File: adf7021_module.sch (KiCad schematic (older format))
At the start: 39 parts

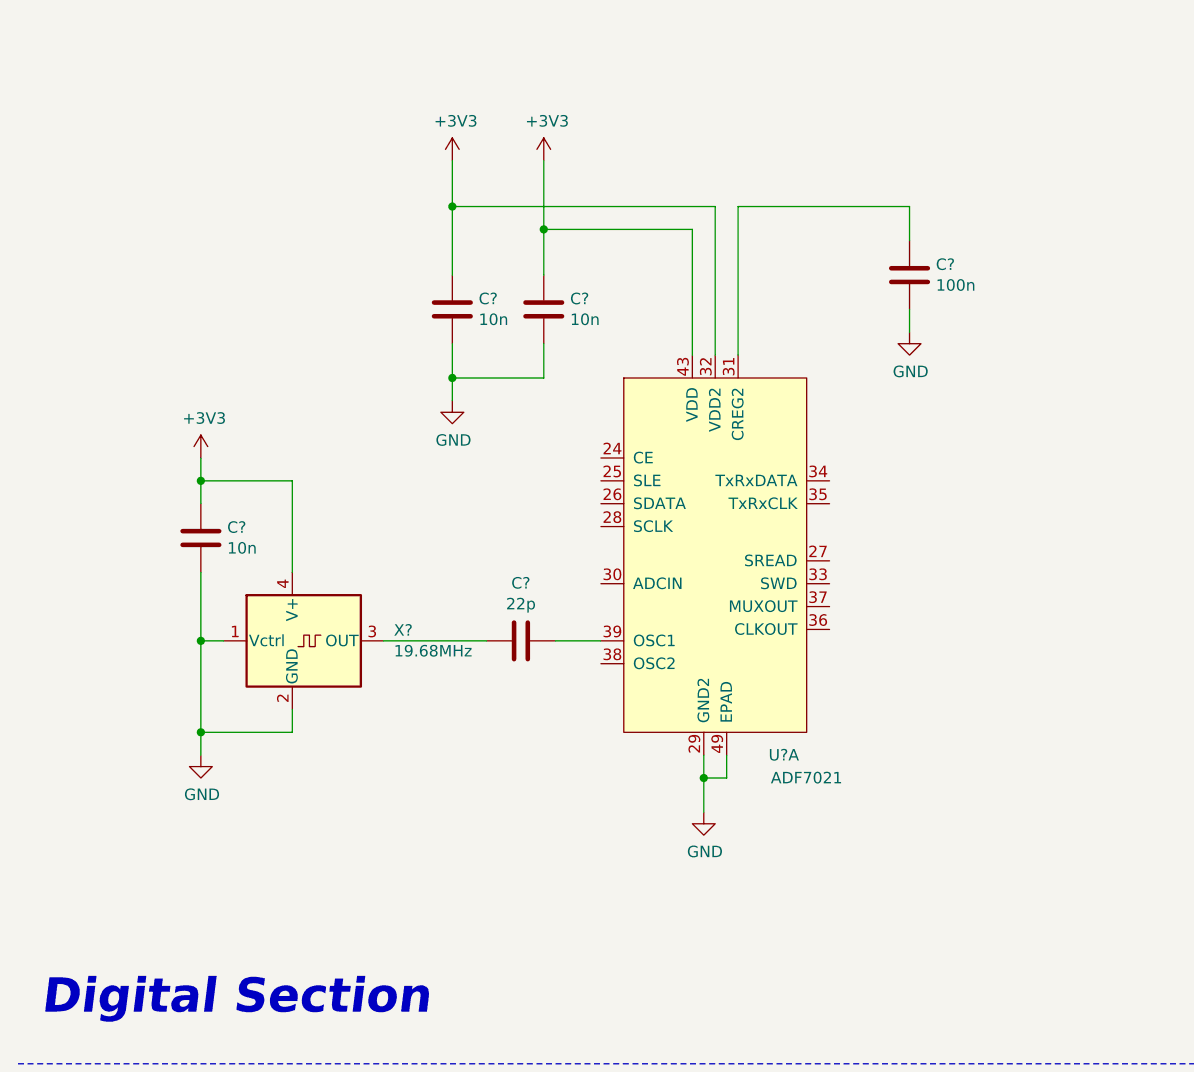
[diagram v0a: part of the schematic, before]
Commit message: Add external clock input SMA
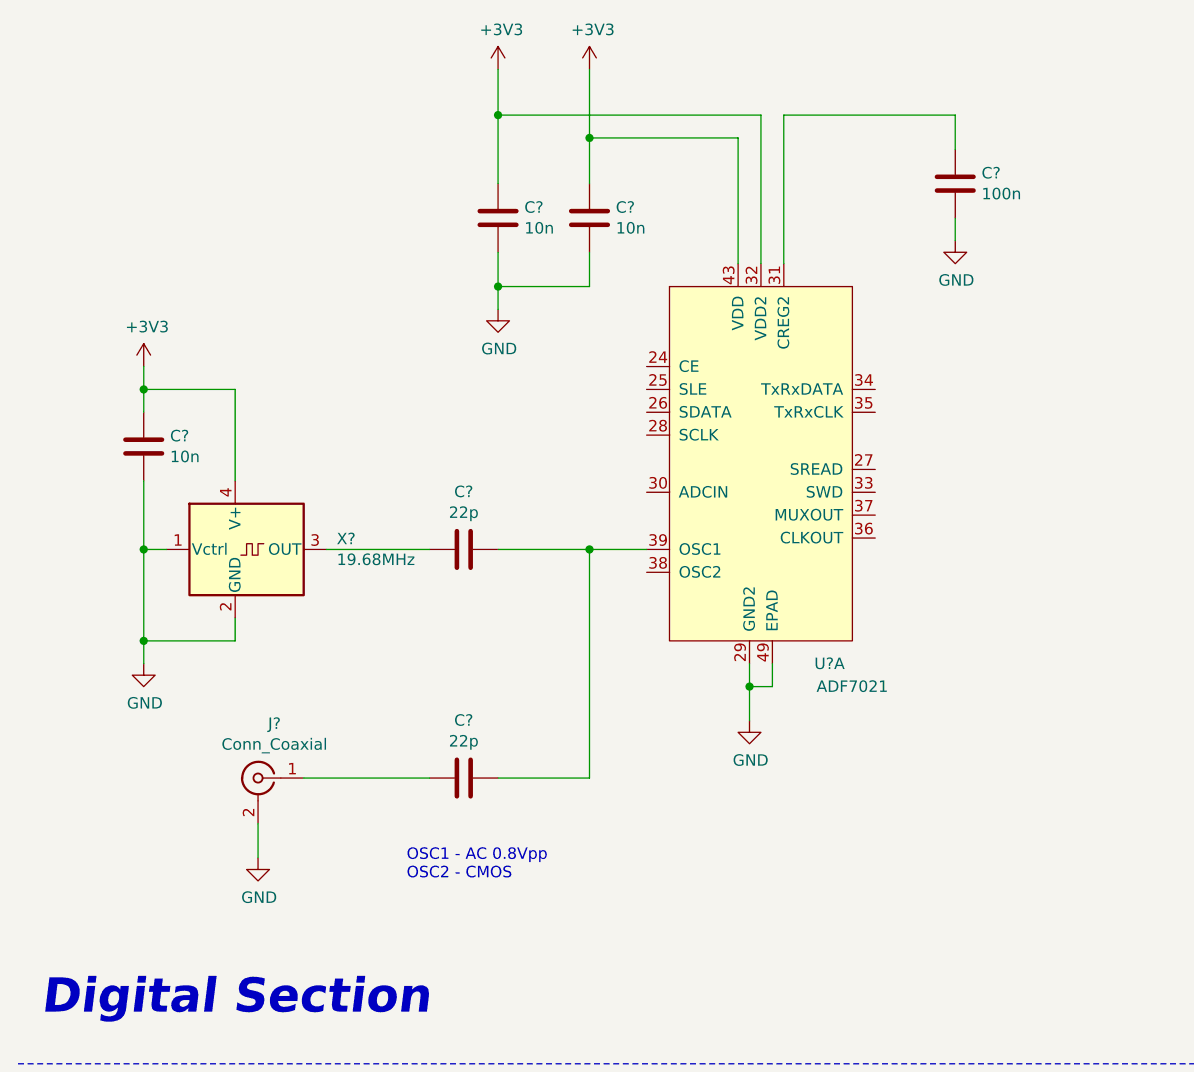
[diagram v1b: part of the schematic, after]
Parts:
- added C?: 22p, symbol Device:C
- added J?: Conn_Coaxial, symbol Connector:Conn_Coaxial
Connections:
- net GND: now also J?.2 (Ext)
- net at C?.1, U?.39 (OSC1): now also C?.1
- new net: C?.2, J?.1 (In)
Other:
- note added: "OSC1 - AC 0.8Vpp\nOSC2 - CMOS"
- moved on the sheet: C?, U?A, X?

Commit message: RF output chain, labels for digital pins
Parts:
- removed J?: Conn_Coaxial, symbol Connector:Conn_Coaxial
- added C16: 100n, symbol Device:C
- added C17: 2.2n, symbol Device:C
- added C18: 10p, symbol Device:C
- added C23, C25: DNP, symbol Device:C
- added C24: 6.8p, symbol Device:C
- added C26, C27: 4.7p, symbol Device:C
- added J2: Conn_Coaxial, symbol Connector:Conn_Coaxial
- added L2: 20n, symbol Device:L
- added L3: 22n, symbol Device:L
- added R4: 100, symbol Device:R
- added R5, R6: 47k, symbol Device:R
- added R7: 22k, symbol Device:R
- gave numbers to parts that had none: 38
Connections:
- net RFIN is gone; now on an unnamed net: C30.2
- net GND: now also C17.1, C23.2, C24.2, C25.2, J2.2 (Ext), R7.1
- net VCOIN: now also R4.1, R5.2; no longer C12.1, R2.2
- net at C15.2: now also C9.1, U1.39 (OSC1)
- net CE: now reaches U1.24 (CE)
- net SLE: now reaches U1.25 (SLE)
- net SDATA: now reaches U1.26 (SDATA)
- net SREAD: now reaches U1.27 (SREAD)
- net SCLK: now reaches U1.28 (SCLK)
- net ADCIN: now reaches U1.30 (ADCIN)
- net SWD: now reaches U1.33 (SWD)
- net TxRxData: now reaches U1.34 (TxRxDATA)
- net TxRxCLK: now reaches U1.35 (TxRxCLK)
- net CLKOUT: now reaches U1.36 (CLKOUT)
- net MUXOUT: now reaches U1.37 (MUXOUT)
- net at C19.2, L4.2, U1.4 (RFOUT): now also C18.2
- net at L5.2, U1.6 (RFIN): now also C26.1, C27.1; no longer C30.1
- net at C33.1, J3.1 (In), L7.1: now also C27.2
- net at C31.1, L6.2: now also C30.1
- net RFOUT: no longer names the net of C19.1
- net RFOUT: now also C23.1, C26.2, L2.2
- new net: C18.1, C25.1, J2.1 (In), L3.1
- new net: C24.1, L2.1, L3.2
- new net: C12.1, R2.2, R4.2
- new net: C16.2, R5.1
- new net: C16.1, C17.2, R6.2
- new net CLK_AC_IN: C15.1
- new net FM_MOD: R6.1, R7.2
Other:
- note added: "C18, C19 are "multiplexer"\nDC blocking caps. Place one."
- note added: "C26, C27, C30 are "multiplexer"\nDC blocking caps. Place one."
- note added: "Input 3Vp-p\nSet deviation with R5"
- note added: "OSC1 - AC 0.8Vp-p\nOSC2 - CMOS"
- note removed: "OSC1 - AC 0.8Vpp\nOSC2 - CMOS"
- moved on the sheet: C10, C11, C12, C13, C14, C15, C19, C2, C20, C21, C22, C28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

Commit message: Improving documentation on schematic
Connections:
- net RFIN: now reaches C26.1, C27.1, C30.2, L5.2, U1.6 (RFIN)
- net RFOUT: now reaches C18.2, C19.2, L4.2, U1.4 (RFOUT)
- net CLK_DC_IN: now reaches U1.38 (OSC2)
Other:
- note added: "C18, C19 are "multiplexer"\nDC blocking caps. Place one.\n\nC18 - Bypass\nC19 - Filter output"
- note added: "C26, C27, C30 are "multiplexer"\nDC blocking caps. Place one.\n\nC26 - Shared Tx/Rx\nC27 - Bypass Rx\nC30 - Filter Rx"
- note added: "C9, C15 are "multiplexer"\nDC blocking caps. Place one.\n\nC9 - TXCO Input\nC15 - External Input"
- note added: "Harmonic filter values taken from EVAL-ADF7021DBZ3\nmodule. (For 431 MHz - 470 MHz)\n\n3 dB @ 730 MHz"
- note removed: "3 dB @ 730 MHz"
- note removed: "C18, C19 are "multiplexer"\nDC blocking caps. Place one."
- note removed: "C26, C27, C30 are "multiplexer"\nDC blocking caps. Place one."
- note removed: "Harmonic filter values taken from EVAL-ADF7021DBZ3\nmodule. (For 431 MHz - 470 MHz)"
- moved on the sheet: C15, C9
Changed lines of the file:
@@
 AR Path="/5FB73817/6009402F" Ref="X?"  Part="1"
 AR Path="/6009402F" Ref="X1"  Part="1"
-F 0 "X1" H 1694 3296 50  0000 L CNN
-F 1 "19.68MHz" H 1694 3205 50  0000 L CNN
+F 0 "X1" H 1350 3650 50  0000 L CNN
+F 1 "19.68MHz" H 1350 3550 50  0000 L CNN
 F 2 "Oscillator:Oscillator_SMD_Fordahl_DFAS2-4Pin_7.3x5.1mm" H 2350 2900 50  0001 C CNN
 F 3 "http://www.metatech.com.hk/product/fordahl/pdf/2002%20TCXO%20Page%2043-58.pdf" H 1150 3250 50  0001 C CNN
@@
 L Device:C C?
 U 1 1 60094035
-P 2250 3250
+P 2150 3250
 AR Path="/5FB73817/60094035" Ref="C?"  Part="1"
 AR Path="/60094035" Ref="C9"  Part="1"
-F 0 "C9" V 1998 3250 50  0000 C CNN
-F 1 "22p" V 2089 3250 50  0000 C CNN
-F 2 "" H 2288 3100 50  0001 C CNN
-F 3 "~" H 2250 3250 50  0001 C CNN
-	1    2250 3250
+F 0 "C9" V 1898 3250 50  0000 C CNN
+F 1 "22p" V 1989 3250 50  0000 C CNN
+F 2 "" H 2188 3100 50  0001 C CNN
+F 3 "~" H 2150 3250 50  0001 C CNN
+	1    2150 3250
 	0    1    1    0
 $EndComp
-Wire Wire Line
-	1650 3250 2100 3250
 $Comp
 L power:+3V3 #PWR?
@@
 	9400 9150 9400 9550
 Connection ~ 9400 9550
-Text Notes 8750 8650 2    50   ~ 0
-3 dB @ 730 MHz
 Wire Notes Line
 	6700 1000 6700 5500
@@
 Text Notes 9900 4600 0    50   Italic 0
 Loop filter taken from EVAL-ADF7021DBZ3\nmodule. (For 431 MHz - 470 MHz)
-Text Notes 9300 6000 2    50   Italic 0
-Harmonic filter values taken from EVAL-ADF7021DBZ3\nmodule. (For 431 MHz - 470 MHz)
+Text Notes 7000 10050 0    50   Italic 0
+Harmonic filter values taken from EVAL-ADF7021DBZ3\nmodule. (For 431 MHz - 470 MHz)\n\n3 dB @ 730 MHz
 Text Notes 2000 9850 0    50   Italic 0
 Matching network taken from EVAL-ADF7021DBZ3\nmodule. (For 431 MHz - 470 MHz)
@@
 L Device:C C?
 U 1 1 5FC62852
-P 2600 3500
+P 2450 3500
 AR Path="/5FB73817/5FC62852" Ref="C?"  Part="1"
 AR Path="/5FC62852" Ref="C15"  Part="1"
-F 0 "C15" V 2348 3500 50  0000 C CNN
-F 1 "22p" V 2439 3500 50  0000 C CNN
-F 2 "" H 2638 3350 50  0001 C CNN
-F 3 "~" H 2600 3500 50  0001 C CNN
-	1    2600 3500
+F 0 "C15" V 2198 3500 50  0000 C CNN
+F 1 "22p" V 2289 3500 50  0000 C CNN
+F 2 "" H 2488 3350 50  0001 C CNN
+F 3 "~" H 2450 3500 50  0001 C CNN
+	1    2450 3500
 	-1   0    0    1
 $EndComp
-Text Notes 2550 4700 0    50   ~ 0
+Text Notes 2200 4350 0    50   ~ 0
 OSC1 - AC 0.8Vp-p\nOSC2 - CMOS
 $Comp
@@
 	14400 4400 14700 4400
 Connection ~ 14400 4400
-Text Label 14700 4400 0    50   ~ 0
-FM_MOD
 Text Notes 14650 4200 0    50   ~ 0
 Input 3Vp-p\nSet deviation with R5
@@
 	9400 7250 9400 7650
 Connection ~ 9400 7650
-Text Notes 8750 6750 2    50   ~ 0
-3 dB @ 730 MHz
 Wire Wire Line
 	6000 7900 6000 7050
@@
 	1250 7850 1250 10150
 Wire Wire Line
-	1250 10150 6050 10150
-Wire Wire Line
-	6050 10150 6050 8950
-Wire Wire Line
-	6050 8950 6450 8950
+	1250 10150 5800 10150
+Wire Wire Line
+	5800 10150 5800 8950
+Wire Wire Line
+	5800 8950 6450 8950
 Connection ~ 7300 8950
 Wire Wire Line
@@
 Wire Wire Line
 	9000 7050 8700 7050
-Text Notes 6350 10150 0    50   ~ 0
-C26, C27, C30 are "multiplexer"\nDC blocking caps. Place one.
-Text Notes 5850 6000 0    50   ~ 0
-C18, C19 are "multiplexer"\nDC blocking caps. Place one.
-Wire Wire Line
-	2600 3250 3600 3250
-Wire Wire Line
-	2400 3250 2600 3250
-Connection ~ 2600 3250
-Wire Wire Line
-	2600 3350 2600 3250
-Wire Wire Line
-	2600 3650 2600 3750
-Wire Wire Line
-	2600 3750 2000 3750
+Text Notes 6100 9650 0    30   ~ 0
+C26, C27, C30 are "multiplexer"\nDC blocking caps. Place one.\n\nC26 - Shared Tx/Rx\nC27 - Bypass Rx\nC30 - Filter Rx
+Text Notes 5800 6100 0    30   ~ 0
+C18, C19 are "multiplexer"\nDC blocking caps. Place one.\n\nC18 - Bypass\nC19 - Filter output
+Wire Wire Line
+	2450 3250 3600 3250
+Wire Wire Line
+	2300 3250 2450 3250
+Connection ~ 2450 3250
+Wire Wire Line
+	2450 3350 2450 3250
+Wire Wire Line
+	2450 3650 2450 3750
+Wire Wire Line
+	2450 3750 2000 3750
 Text GLabel 2000 3750 0    50   Input ~ 0
 CLK_AC_IN
@@
 Wire Wire Line
 	4600 2900 4850 2900
+Text GLabel 2000 3950 0    50   Input ~ 0
+CLK_DC_IN
+Wire Wire Line
+	2000 3950 2850 3950
+Wire Wire Line
+	2850 3950 2850 3350
+Wire Wire Line
+	2850 3350 3600 3350
+Text GLabel 14700 4400 2    50   Input ~ 0
+FM_MOD
+Text Notes 2000 2900 0    30   ~ 0
+C9, C15 are "multiplexer"\nDC blocking caps. Place one.\n\nC9 - TXCO Input\nC15 - External Input
+Wire Wire Line
+	1650 3250 2000 3250
+Wire Notes Line
+	1950 3650 2750 3650
+Wire Notes Line
+	2750 3650 2750 2950
+Wire Notes Line
+	2750 2950 1950 2950
+Wire Notes Line
+	1950 2950 1950 3650
+Wire Notes Line
+	5800 6150 5800 7200
+Wire Notes Line
+	5800 7200 6500 7200
+Wire Notes Line
+	6500 7200 6500 6150
+Wire Notes Line
+	6500 6150 5800 6150
+Wire Notes Line
+	6100 8100 6100 9300
+Wire Notes Line
+	6100 9300 6850 9300
+Wire Notes Line
+	6850 9300 6850 8100
+Wire Notes Line
+	6850 8100 6100 8100
+Text Label 1500 7850 0    50   ~ 0
+RFIN
+Text Label 5150 7900 0    50   ~ 0
+RFOUT
 $EndSCHEMATC

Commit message: Adding 2x10 data headers, unifying CLK_IN signal
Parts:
- added C?: 10u, symbol Device:C
- added C?: 4.7u, symbol Device:C
- added C?: 1u, symbol Device:C
- added J1, J?: Conn_02x10_Counter_Clockwise, symbol Connector_Generic:Conn_02x10_Counter_Clockwise
- added R10: 0, symbol Device:R
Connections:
- net +3V3: now also C?.1, C?.1, C?.1, J1.1 (Pin_1), J1.20 (Pin_20), J?.1 (Pin_1), J?.20 (Pin_20)
- net ADCIN: now also J1.19 (Pin_19), J?.19 (Pin_19)
- net CE: now also J1.3 (Pin_3), J?.3 (Pin_3)
- net CLKOUT: now also J1.11 (Pin_11), J?.11 (Pin_11)
- net FM_MOD: now also J1.2 (Pin_2), J?.2 (Pin_2)
- net GND: now also C?.2, C?.2, C?.2, J1.12 (Pin_12), J1.16 (Pin_16), J1.5 (Pin_5), J1.8 (Pin_8), J1.9 (Pin_9), J?.12 (Pin_12), J?.16 (Pin_16), J?.5 (Pin_5), J?.8 (Pin_8), J?.9 (Pin_9)
- net MUXOUT: now also J1.17 (Pin_17), J?.17 (Pin_17)
- net SCLK: now also J1.7 (Pin_7), J?.7 (Pin_7)
- net SDATA: now also J1.6 (Pin_6), J?.6 (Pin_6)
- net SLE: now also J1.4 (Pin_4), J?.4 (Pin_4)
- net SREAD: now also J1.15 (Pin_15), J?.15 (Pin_15)
- net SWD: now also J1.18 (Pin_18), J?.18 (Pin_18)
- net TxRxCLK: now also J1.13 (Pin_13), J?.13 (Pin_13)
- net TxRxData: now also J1.14 (Pin_14), J?.14 (Pin_14)
- net CLK_AC_IN renamed CLK_IN
- net CLK_IN: now also J1.10 (Pin_10), J?.10 (Pin_10), R10.2
- net CLK_DC_IN: no longer names the net of U1.38 (OSC2)
- net CLK_DC_IN: now also R10.1
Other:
- note added: "Analog\nLow Speed"
- note added: "C9, C15, R10 are "multiplexer"\nparts. Place one.\n\nC9 - TXCO AC Input\nC15 - External AC Input\nR10 - External CMOS Input"
- note added: "Clocks"
- note added: "Data / SPI"
- note added: "I/O Section"
- note removed: "C9, C15 are "multiplexer"\nDC blocking caps. Place one.\n\nC9 - TXCO Input\nC15 - External Input"

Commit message: Annotating parts
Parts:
- gave numbers to parts that had none: 4
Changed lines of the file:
@@
 P 11000 6550
 AR Path="/5FB73817/604945F1" Ref="#PWR?"  Part="1"
-AR Path="/604945F1" Ref="#PWR?"  Part="1"
-F 0 "#PWR?" H 11000 6400 50  0001 C CNN
+AR Path="/604945F1" Ref="#PWR030"  Part="1"
+F 0 "#PWR030" H 11000 6400 50  0001 C CNN
 F 1 "+3V3" H 11015 6723 50  0000 C CNN
 F 2 "" H 11000 6550 50  0001 C CNN
@@
 	11450 7250 11550 7250
 $Comp
-L Device:C C?
+L Device:C C34
 U 1 1 605431F6
 P 14200 6950
-F 0 "C?" H 14315 6996 50  0000 L CNN
+F 0 "C34" H 14315 6996 50  0000 L CNN
 F 1 "10u" H 14315 6905 50  0000 L CNN
 F 2 "" H 14238 6800 50  0001 C CNN
@@
 $EndComp
 $Comp
-L Device:C C?
+L Device:C C35
 U 1 1 60543C1C
 P 14600 6950
-F 0 "C?" H 14715 6996 50  0000 L CNN
+F 0 "C35" H 14715 6996 50  0000 L CNN
 F 1 "4.7u" H 14715 6905 50  0000 L CNN
 F 2 "" H 14638 6800 50  0001 C CNN
@@
 $EndComp
 $Comp
-L Device:C C?
+L Device:C C36
 U 1 1 60543F9A
 P 15000 6950
-F 0 "C?" H 15115 6996 50  0000 L CNN
+F 0 "C36" H 15115 6996 50  0000 L CNN
 F 1 "1u" H 15115 6905 50  0000 L CNN
 F 2 "" H 15038 6800 50  0001 C CNN
@@
 $EndComp
 $Comp
-L power:GND #PWR?
+L power:GND #PWR033
 U 1 1 60544BDA
 P 14200 7250
-F 0 "#PWR?" H 14200 7000 50  0001 C CNN
+F 0 "#PWR033" H 14200 7000 50  0001 C CNN
 F 1 "GND" H 14205 7077 50  0000 C CNN
 F 2 "" H 14200 7250 50  0001 C CNN
@@
 P 14200 6600
 AR Path="/5FB73817/6057B9B9" Ref="#PWR?"  Part="1"
-AR Path="/6057B9B9" Ref="#PWR?"  Part="1"
-F 0 "#PWR?" H 14200 6450 50  0001 C CNN
+AR Path="/6057B9B9" Ref="#PWR032"  Part="1"
+F 0 "#PWR032" H 14200 6450 50  0001 C CNN
 F 1 "+3V3" H 14215 6773 50  0000 C CNN
 F 2 "" H 14200 6600 50  0001 C CNN
@@
 CLK_IN
 $Comp
-L Connector_Generic:Conn_02x10_Counter_Clockwise J?
+L Connector_Generic:Conn_02x10_Counter_Clockwise J4
 U 1 1 605D2305
 P 11750 8300
-F 0 "J?" H 11800 8917 50  0000 C CNN
+F 0 "J4" H 11800 8917 50  0000 C CNN
 F 1 "Conn_02x10_Counter_Clockwise" H 11800 8826 50  0000 C CNN
 F 2 "" H 11750 8300 50  0001 C CNN
@@
 	12350 8100 12050 8100
 $Comp
-L power:GND #PWR?
+L power:GND #PWR037
 U 1 1 605D230F
 P 12800 8300
-F 0 "#PWR?" H 12800 8050 50  0001 C CNN
+F 0 "#PWR037" H 12800 8050 50  0001 C CNN
 F 1 "GND" V 12805 8172 50  0000 R CNN
 F 2 "" H 12800 8300 50  0001 C CNN
@@
 	11250 8500 11550 8500
 $Comp
-L power:GND #PWR?
+L power:GND #PWR038
 U 1 1 605D2318
 P 11000 8600
-F 0 "#PWR?" H 11000 8350 50  0001 C CNN
+F 0 "#PWR038" H 11000 8350 50  0001 C CNN
 F 1 "GND" V 11005 8472 50  0000 R CNN
 F 2 "" H 11000 8600 50  0001 C CNN
@@
 	11000 8600 11450 8600
 $Comp
-L power:GND #PWR?
+L power:GND #PWR036
 U 1 1 605D231F
 P 11000 8300
-F 0 "#PWR?" H 11000 8050 50  0001 C CNN
+F 0 "#PWR036" H 11000 8050 50  0001 C CNN
 F 1 "GND" V 11005 8172 50  0000 R CNN
 F 2 "" H 11000 8300 50  0001 C CNN
@@
 	11000 8300 11550 8300
 $Comp
-L power:GND #PWR?
+L power:GND #PWR039
 U 1 1 605D2326
 P 12800 8700
-F 0 "#PWR?" H 12800 8450 50  0001 C CNN
+F 0 "#PWR039" H 12800 8450 50  0001 C CNN
 F 1 "GND" V 12805 8572 50  0000 R CNN
 F 2 "" H 12800 8700 50  0001 C CNN
@@
 P 12800 7900
 AR Path="/5FB73817/605D2335" Ref="#PWR?"  Part="1"
-AR Path="/605D2335" Ref="#PWR?"  Part="1"
-F 0 "#PWR?" H 12800 7750 50  0001 C CNN
+AR Path="/605D2335" Ref="#PWR035"  Part="1"
+F 0 "#PWR035" H 12800 7750 50  0001 C CNN
 F 1 "+3V3" H 12815 8073 50  0000 C CNN
 F 2 "" H 12800 7900 50  0001 C CNN
@@
 P 11000 7900
 AR Path="/5FB73817/605D233C" Ref="#PWR?"  Part="1"
-AR Path="/605D233C" Ref="#PWR?"  Part="1"
-F 0 "#PWR?" H 11000 7750 50  0001 C CNN
+AR Path="/605D233C" Ref="#PWR034"  Part="1"
+F 0 "#PWR034" H 11000 7750 50  0001 C CNN
 F 1 "+3V3" H 11015 8073 50  0000 C CNN
 F 2 "" H 11000 7900 50  0001 C CNN
